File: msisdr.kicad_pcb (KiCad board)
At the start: 2 copper layers, 46.3 x 90.7 mm, 70 parts, among them J1 VCC_GPIO, J10 SMA_VHF1, J11 USB_OTG, J2 GPIO0, J3 GPIO1, J4 GPIO2, J5 GPIO3, J6 SMA_0_30MHZ, J7 SMA_30_60MHZ, J8 SMA_VHF2, J9 SMA_UHF, U1 msi2500, U2 msi001, U3 LP5900SDX-2.8, U4 AP7313-30SAG, Y1 24MHz

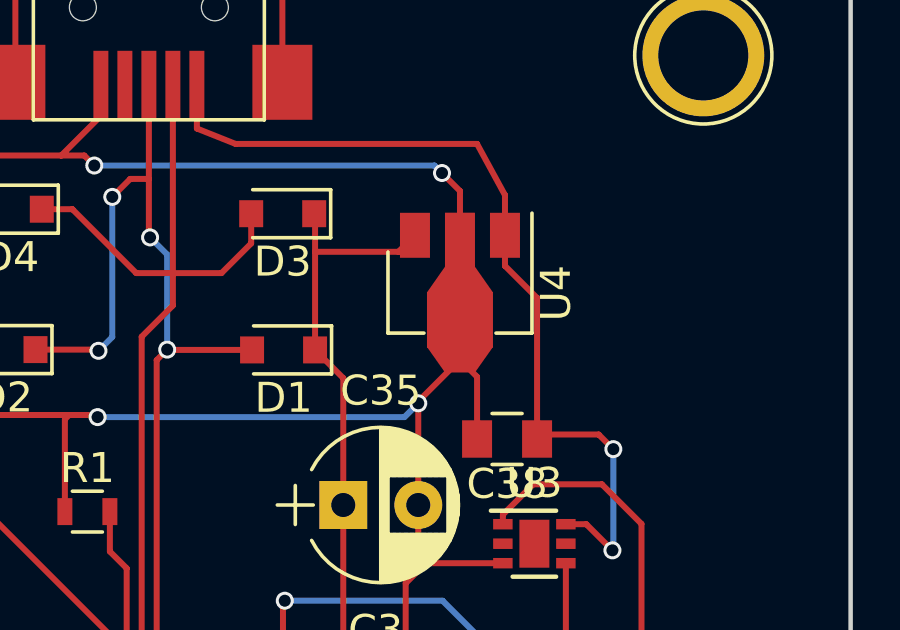
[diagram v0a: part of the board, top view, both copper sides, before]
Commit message: fix ldo ap7313 bug
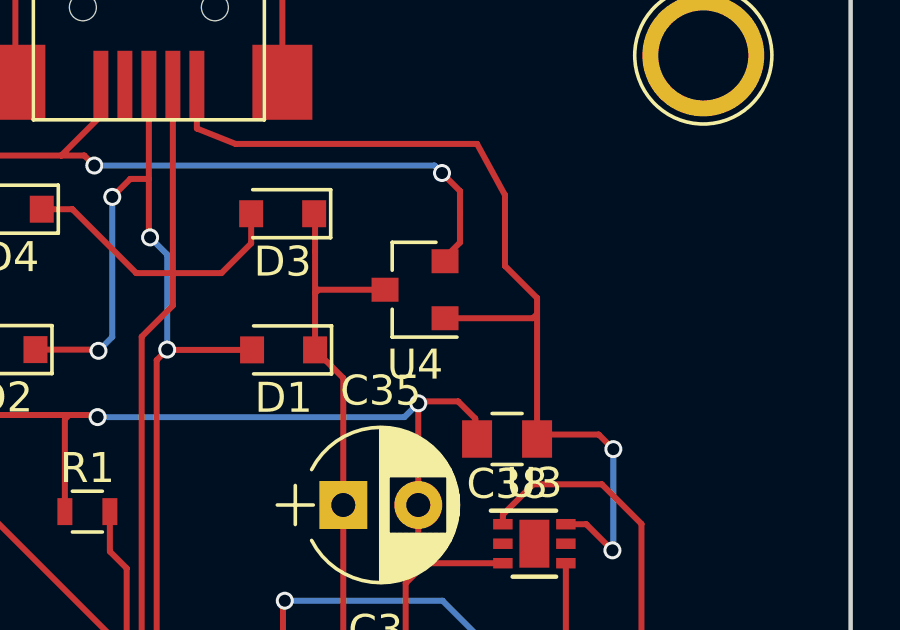
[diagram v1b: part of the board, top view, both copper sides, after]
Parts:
- U4: footprint TO_SOT_Packages_SMD:SOT-89-3 -> TO_SOT_Packages_SMD:SOT-23
- moved U4 1.54 mm to (144.9, 57.8), turned to 180 degrees
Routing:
- net GND: track 398.2 -> 393.2 mm
- net Net-(C38-Pad1): track 29.5 -> 32.6 mm
- net VDIG: track 105.7 -> 104.5 mm
